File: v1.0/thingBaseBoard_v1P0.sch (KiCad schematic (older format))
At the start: 61 parts, among them P1 AC_230V, P2 TOUCH_PANEL_CONNECTOR, P3 APPLIANCES_CONNECTOR, Q1 2N3904-MMBT, Q2 2N3904-MMBT, Q3 2N3904-MMBT, Q4 2N3904-MMBT, Q5 2N3904-MMBT, Q6 2N3904-MMBT, Q7 2N7002, U1 HenLv-AC220S3_3DCS-3W, U2 DF08S1_BRIDGE_REC-IC, U3 XBEE_MODULE, U4 TRIAC_BOARD, U5 4N35_OPTO, U6 TRIAC_BOARD

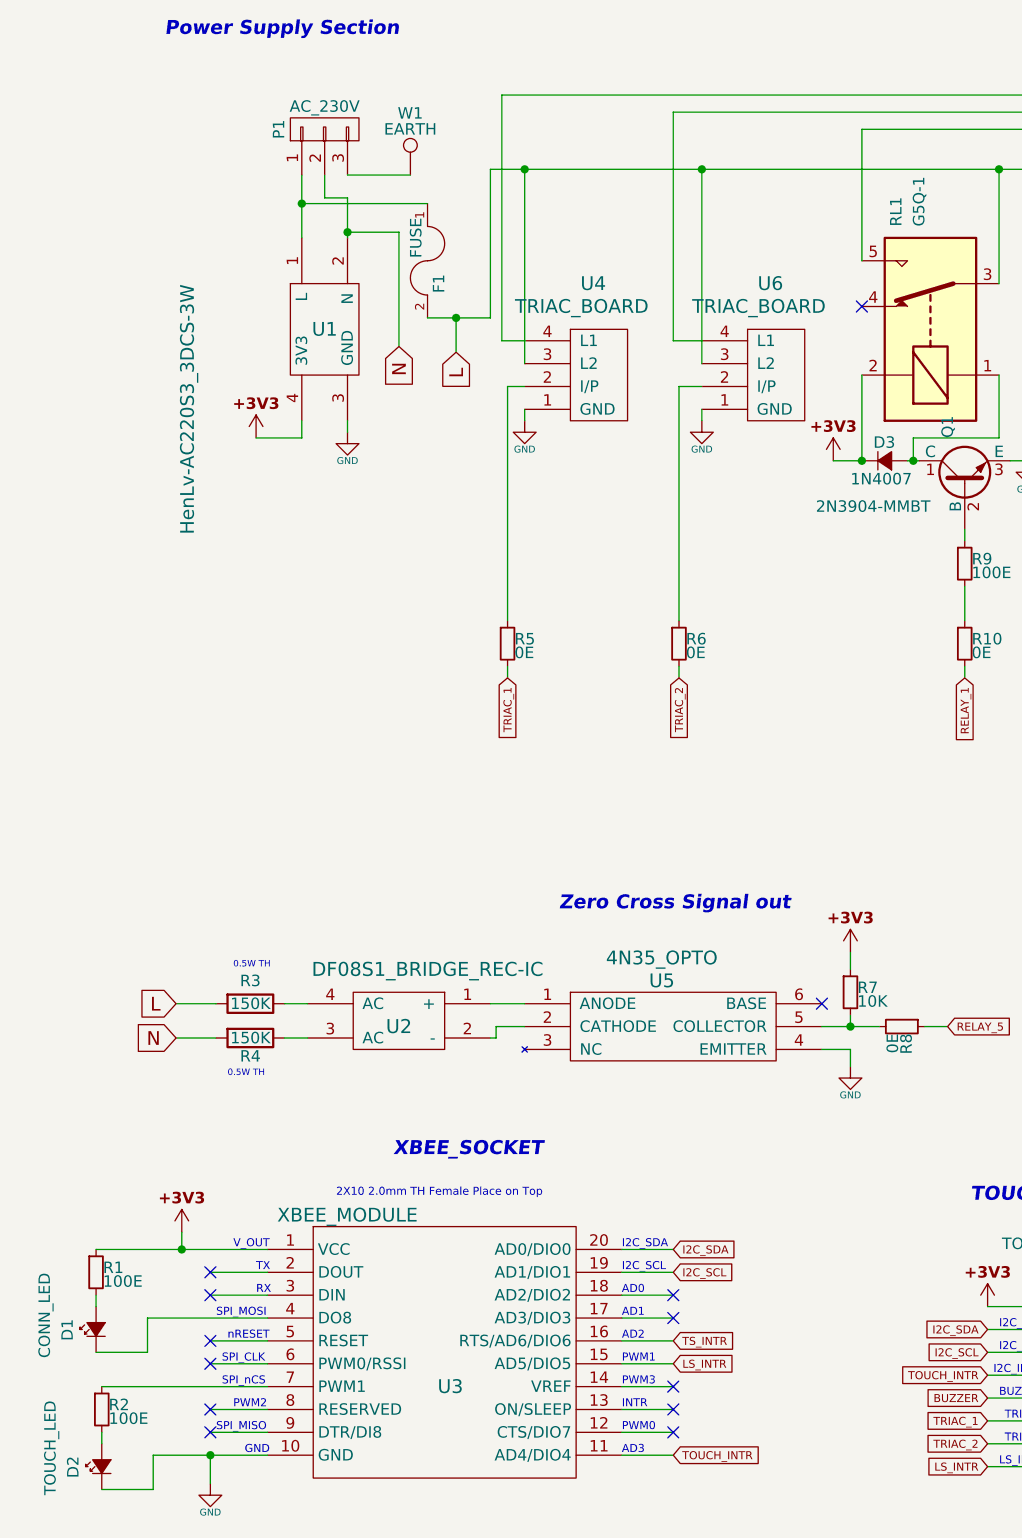
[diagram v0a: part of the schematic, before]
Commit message: All footprints are placed in Layout
All footprints are placed in Layout
- silk Screen Added for all
- size of the Pcb decreased by 2mm
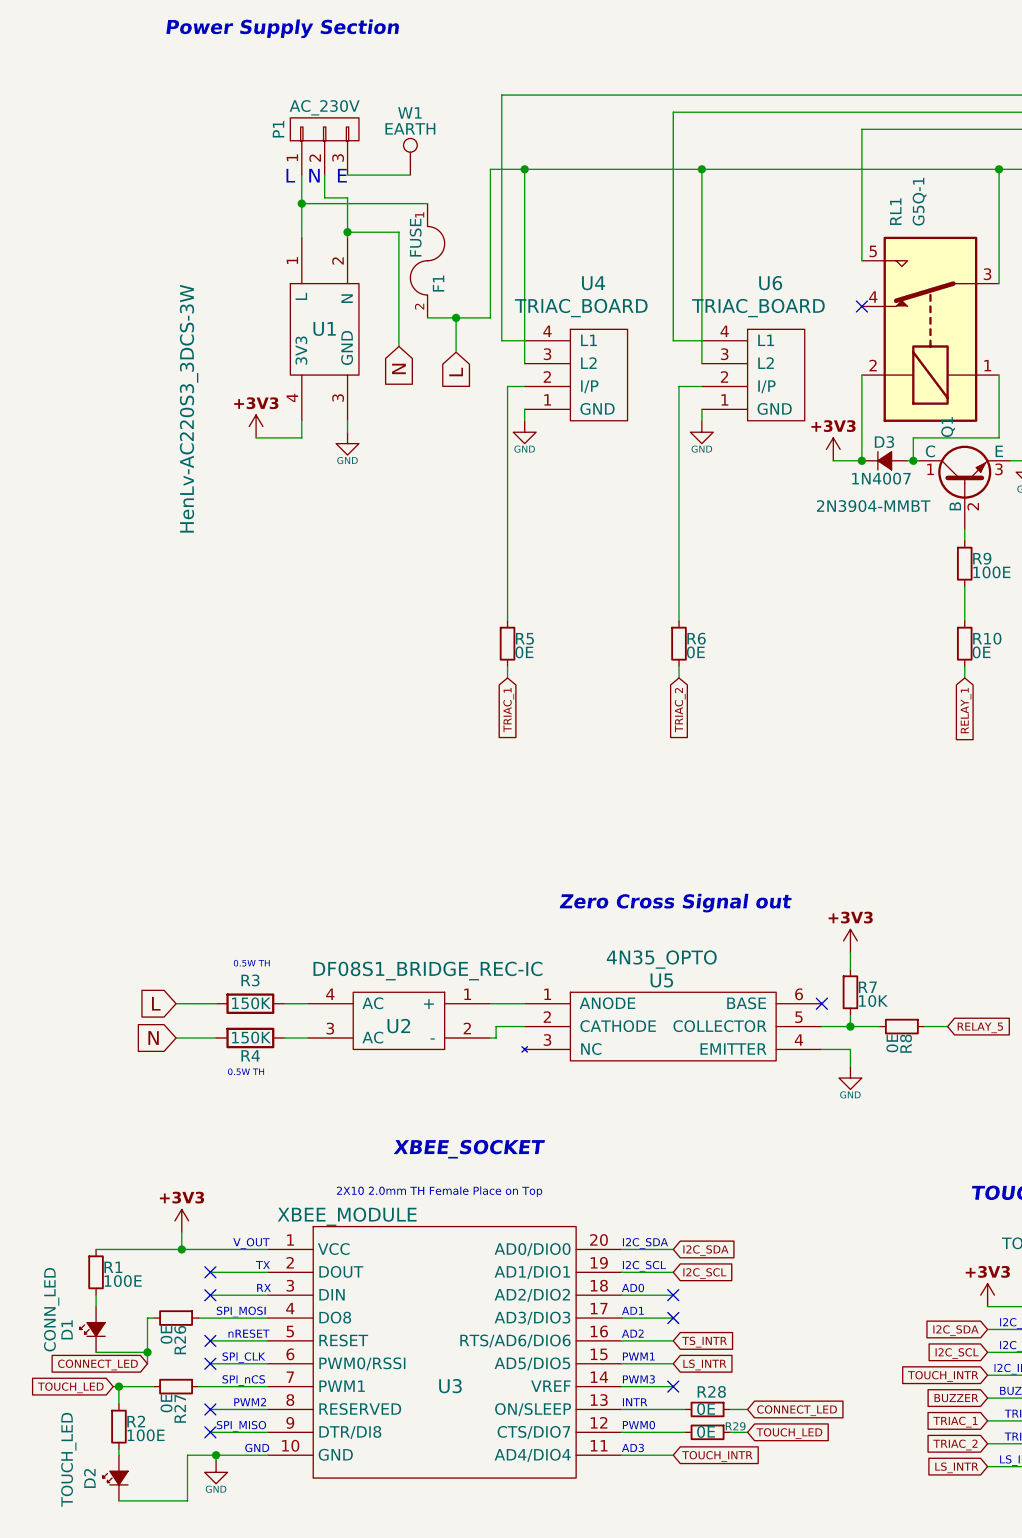
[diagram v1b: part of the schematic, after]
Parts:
- added R26, R27, R28, R29: 0E, Resistors_SMD:R_0805_HandSoldering, symbol R_Small
- C1: footprint (none) -> Capacitors_SMD:C_0805_HandSoldering
- D1, D2, D8: footprint (none) -> LEDs:LED_0805
- D10, D3, D4, D5, D6, D7, D9: footprint (none) -> Diodes_SMD:D_0805
- F1: footprint (none) -> Fuse:8mm_Pitch
- P1: footprint (none) -> Connectors:gmkds_3-3-5,08
- P2: footprint (none) -> Connectors:IDC_Header_Straight_16pins
- P3: footprint (none) -> Connectors:gmkds_3-8-5,08
- Q1, Q2, Q3, Q4, Q5, Q6: footprint TO-92 -> TO_SOT_Packages_SMD:TSOT-23
- Q7: footprint (none) -> TO_SOT_Packages_SMD:SOT-23
- R1, R10, R11, R12, R13, R14, R15, R16, R17, R18, R19, R2, R20, R21, R22, R23, R24, R25, R5, R6, R7, R8, R9: footprint (none) -> Resistors_SMD:R_0805_HandSoldering
- R3, R4: footprint (none) -> Resistors_ThroughHole:R_Axial_DIN0309_L9.0mm_D3.2mm_P12.70mm_Horizontal
- RL1, RL2, RL3, RL4, RL5, RL6: footprint Relays_THT:Relay_SPDT_OMRON-G5Q -> relays:Songle_SRS-03VDC-SL
- SP1: footprint (none) -> Buzzers_Beepers:Buzzer_12x9.5RM7.6
- U1: footprint (none) -> HenLv_power_modules:AC220S3.3DCS-3W HenLv
- U2: footprint (none) -> diodes:DF08S1_DIODE_BRIDGE
- U3: footprint (none) -> Xbee:XBee_Socket_without_Jtag
- U4, U6: footprint (none) -> Triac_boards:Triac_board_v1.0
- U5: footprint (none) -> optocoupler:4N35_OPTOCOUPLER
- W1: footprint (none) -> Wire_Pads:SolderWirePad_single_1-2mmDrill
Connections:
- net at U3.12 (CTS/DIO7): now also R29.2
- net at U3.13 (ON/SLEEP): now also R28.2
- net at U3.4 (DO8): now also R26.1; no longer D1.1 (K)
- net at U3.7 (PWM1): now also R27.1; no longer R2.1
- new net CONNECT_LED: D1.1 (K), R26.2, R28.1
- new net TOUCH_LED: R2.1, R27.2, R29.1
- no-connect marks 18 -> 16
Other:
- note added: "E"
- note added: "L"
- note added: "N"
- moved on the sheet: D2, R2

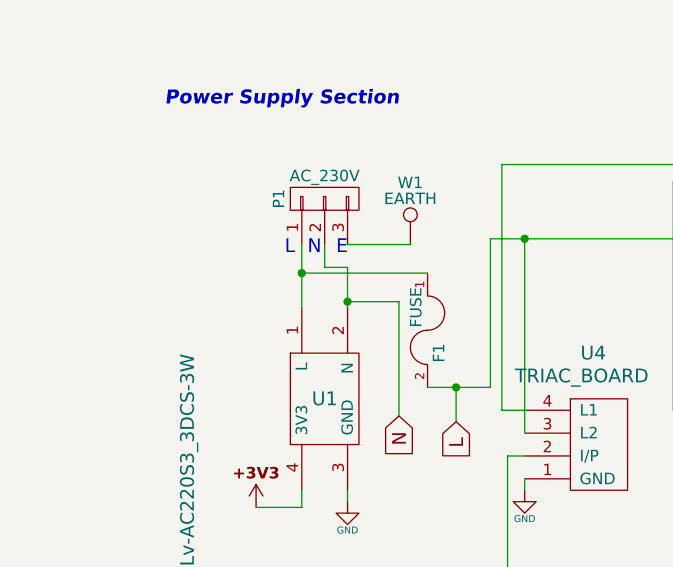
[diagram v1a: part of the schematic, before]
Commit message: Routing done
routing Completed,
Power Module footprint Changed,
2mm size of the PCB reduced.
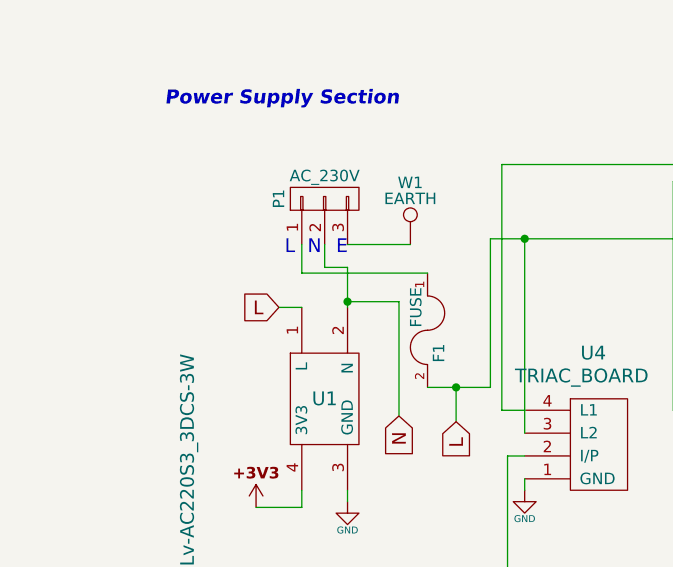
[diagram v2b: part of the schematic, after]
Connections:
- net L: now also U1.1 (L)
- net at F1.1, P1.1 (P1): no longer U1.1 (L)
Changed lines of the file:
@@
 LIBS:df08s1_bridge_rec-ic
 LIBS:4n35_opto
+LIBS:thingBaseBoard_v1P0-cache
 EELAYER 25 0
 EELAYER END
@@
 	0    -1   -1   0
 $EndComp
-Wire Wire Line
-	1700 1825 1700 2100
-Connection ~ 1700 1950
 $Comp
 L CONN_01X08 P3
@@
 	0    1    1    0
 $EndComp
-Wire Wire Line
-	1700 1950 2250 1950
 Wire Wire Line
 	2250 2450 2525 2450
@@
 Wire Wire Line
 	1025 6825 1025 7025
+Text GLabel 1600 2100 0    60   Input ~ 0
+L
+Wire Wire Line
+	1600 2100 1700 2100
+Wire Wire Line
+	1700 1825 1700 1950
+Wire Wire Line
+	1700 1950 2250 1950
 $EndSCHEMATC

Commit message: Bom Create, Holes made in Layout, Schematic Changed
- Bom generated
- in schematic Mosfet Q7 Changed
- in layout mounting holes made
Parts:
- removed Q7: 2N7002, TO_SOT_Packages_SMD:SOT-23, symbol Q_NMOS_DGS
- added Q7: 2N7002, symbol Q_NMOS_GSD
- RL1, RL2, RL3, RL4, RL5, RL6: footprint relays:Songle_SRS-03VDC-SL -> Relays_THT:Relay_SPDT_OMRON-G5Q
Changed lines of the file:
@@
 LIBS:df08s1_bridge_rec-ic
 LIBS:4n35_opto
-LIBS:thingBaseBoard_v1P0-cache
+LIBS:Songle_SRD-03VDC-SL-C
 EELAYER 25 0
 EELAYER END
@@
 $EndComp
 $Comp
-L G5Q-1 RL1
-U 1 1 589421D6
-P 4650 2700
-F 0 "RL1" H 5300 3050 50  0000 L CNN
-F 1 "G5Q-1" H 5300 2950 50  0000 L CNN
-F 2 "relays:Songle_SRS-03VDC-SL" H 5300 2850 50  0001 L CNN
-F 3 "" H 4850 2500 50  0000 C CNN
-	1    4650 2700
-	0    -1   -1   0
-$EndComp
-$Comp
-L G5Q-1 RL2
-U 1 1 58942EA8
-P 5650 2725
-F 0 "RL2" H 6300 3075 50  0000 L CNN
-F 1 "G5Q-1" H 6300 2975 50  0000 L CNN
-F 2 "relays:Songle_SRS-03VDC-SL" H 6300 2875 50  0001 L CNN
-F 3 "" H 5850 2525 50  0000 C CNN
-	1    5650 2725
-	0    -1   -1   0
-$EndComp
-$Comp
-L G5Q-1 RL3
-U 1 1 58942EDF
-P 6675 2750
-F 0 "RL3" H 7325 3100 50  0000 L CNN
-F 1 "G5Q-1" H 7325 3000 50  0000 L CNN
-F 2 "relays:Songle_SRS-03VDC-SL" H 7325 2900 50  0001 L CNN
-F 3 "" H 6875 2550 50  0000 C CNN
-	1    6675 2750
-	0    -1   -1   0
-$EndComp
-$Comp
-L G5Q-1 RL4
-U 1 1 58943019
-P 7600 2750
-F 0 "RL4" H 8250 3100 50  0000 L CNN
-F 1 "G5Q-1" H 8250 3000 50  0000 L CNN
-F 2 "relays:Songle_SRS-03VDC-SL" H 8250 2900 50  0001 L CNN
-F 3 "" H 7800 2550 50  0000 C CNN
-	1    7600 2750
-	0    -1   -1   0
-$EndComp
-$Comp
-L G5Q-1 RL5
-U 1 1 5894305C
-P 8650 2750
-F 0 "RL5" H 9300 3100 50  0000 L CNN
-F 1 "G5Q-1" H 9300 3000 50  0000 L CNN
-F 2 "relays:Songle_SRS-03VDC-SL" H 9300 2900 50  0001 L CNN
-F 3 "" H 8850 2550 50  0000 C CNN
-	1    8650 2750
-	0    -1   -1   0
-$EndComp
-$Comp
 L CONN_01X08 P3
 U 1 1 5894527A
@@
 Wire Wire Line
 	7300 3075 7350 3075
-$Comp
-L G5Q-1 RL6
-U 1 1 58949315
-P 9700 2750
-F 0 "RL6" H 10350 3100 50  0000 L CNN
-F 1 "G5Q-1" H 10350 3000 50  0000 L CNN
-F 2 "relays:Songle_SRS-03VDC-SL" H 10350 2900 50  0001 L CNN
-F 3 "" H 9900 2550 50  0000 C CNN
-	1    9700 2750
-	0    -1   -1   0
-$EndComp
 $Comp
 L BC550 Q6
@@
 Appliances Connector
 $Comp
-L Q_NMOS_DGS Q7
-U 1 1 589FF35C
-P 9875 5775
-F 0 "Q7" H 10175 5825 50  0000 R CNN
-F 1 "2N7002" H 10350 5750 50  0000 R CNN
-F 2 "TO_SOT_Packages_SMD:SOT-23" H 10075 5875 50  0001 C CNN
-F 3 "" H 9875 5775 50  0000 C CNN
-	1    9875 5775
-	1    0    0    -1
-$EndComp
-$Comp
 L D_Small D10
 U 1 1 589C2656
@@
 Wire Wire Line
 	1700 1950 2250 1950
+$Comp
+L Q_NMOS_GSD Q7
+U 1 1 58A75035
+P 9875 5775
+F 0 "Q7" H 10175 5825 50  0000 R CNN
+F 1 "2N7002" H 10350 5725 50  0000 R CNN
+F 2 "" H 10075 5875 50  0000 C CNN
+F 3 "" H 9875 5775 50  0000 C CNN
+	1    9875 5775
+	1    0    0    -1
+$EndComp
+$Comp
+L G5Q-1 RL1
+U 1 1 58A73022
+P 4650 2700
+F 0 "RL1" H 5300 3050 50  0000 L CNN
+F 1 "G5Q-1" H 5300 2950 50  0000 L CNN
+F 2 "Relays_THT:Relay_SPDT_OMRON-G5Q" H 5300 2850 50  0001 L CNN
+F 3 "" H 4850 2500 50  0000 C CNN
+	1    4650 2700
+	0    -1   -1   0
+$EndComp
+$Comp
+L G5Q-1 RL2
+U 1 1 58A7B382
+P 5650 2725
+F 0 "RL2" H 6300 3075 50  0000 L CNN
+F 1 "G5Q-1" H 6300 2975 50  0000 L CNN
+F 2 "Relays_THT:Relay_SPDT_OMRON-G5Q" H 6300 2875 50  0001 L CNN
+F 3 "" H 5850 2525 50  0000 C CNN
+	1    5650 2725
+	0    -1   -1   0
+$EndComp
+$Comp
+L G5Q-1 RL3
+U 1 1 58A7DABA
+P 6675 2750
+F 0 "RL3" H 7325 3100 50  0000 L CNN
+F 1 "G5Q-1" H 7325 3000 50  0000 L CNN
+F 2 "Relays_THT:Relay_SPDT_OMRON-G5Q" H 7325 2900 50  0001 L CNN
+F 3 "" H 6875 2550 50  0000 C CNN
+	1    6675 2750
+	0    -1   -1   0
+$EndComp
+$Comp
+L G5Q-1 RL4
+U 1 1 58A821BC
+P 7600 2750
+F 0 "RL4" H 8250 3100 50  0000 L CNN
+F 1 "G5Q-1" H 8250 3000 50  0000 L CNN
+F 2 "Relays_THT:Relay_SPDT_OMRON-G5Q" H 8250 2900 50  0001 L CNN
+F 3 "" H 7800 2550 50  0000 C CNN
+	1    7600 2750
+	0    -1   -1   0
+$EndComp
+$Comp
+L G5Q-1 RL5
+U 1 1 58A8357F
+P 8650 2750
+F 0 "RL5" H 9300 3100 50  0000 L CNN
+F 1 "G5Q-1" H 9300 3000 50  0000 L CNN
+F 2 "Relays_THT:Relay_SPDT_OMRON-G5Q" H 9300 2900 50  0001 L CNN
+F 3 "" H 8850 2550 50  0000 C CNN
+	1    8650 2750
+	0    -1   -1   0
+$EndComp
+$Comp
+L G5Q-1 RL6
+U 1 1 58A83DF5
+P 9700 2750
+F 0 "RL6" H 10350 3100 50  0000 L CNN
+F 1 "G5Q-1" H 10350 3000 50  0000 L CNN
+F 2 "Relays_THT:Relay_SPDT_OMRON-G5Q" H 10350 2900 50  0001 L CNN
+F 3 "" H 9900 2550 50  0000 C CNN
+	1    9700 2750
+	0    -1   -1   0
+$EndComp
 $EndSCHEMATC
